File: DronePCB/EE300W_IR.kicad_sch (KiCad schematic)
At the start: 18 parts, among them Q4 AO3400A, Q5 AO3400A, U8 TSOP45xx

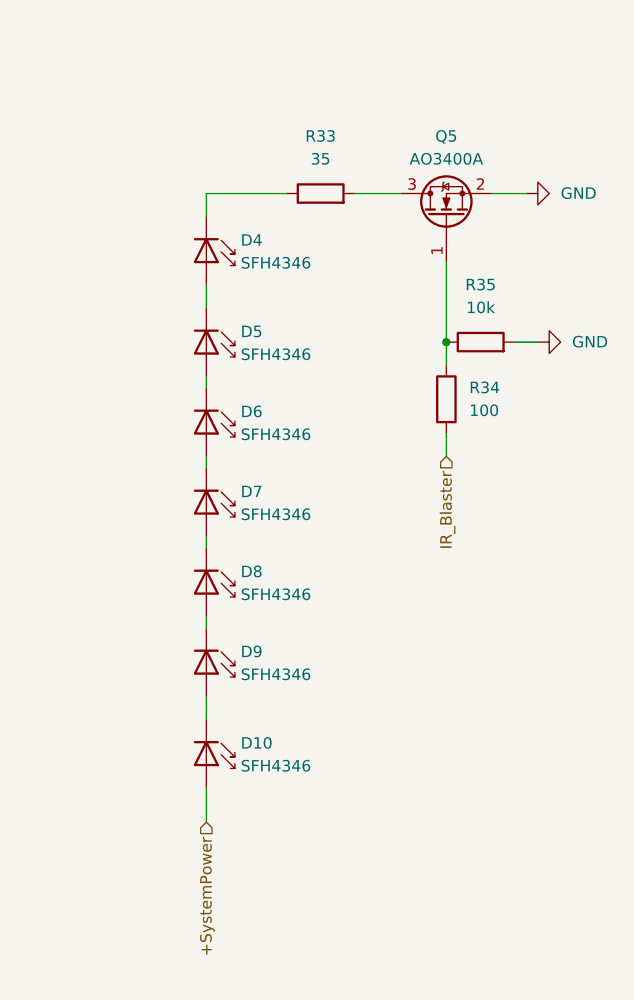
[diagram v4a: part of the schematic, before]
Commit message: Changed Resistor on IR Blaster | Finished Running DRC on PCB
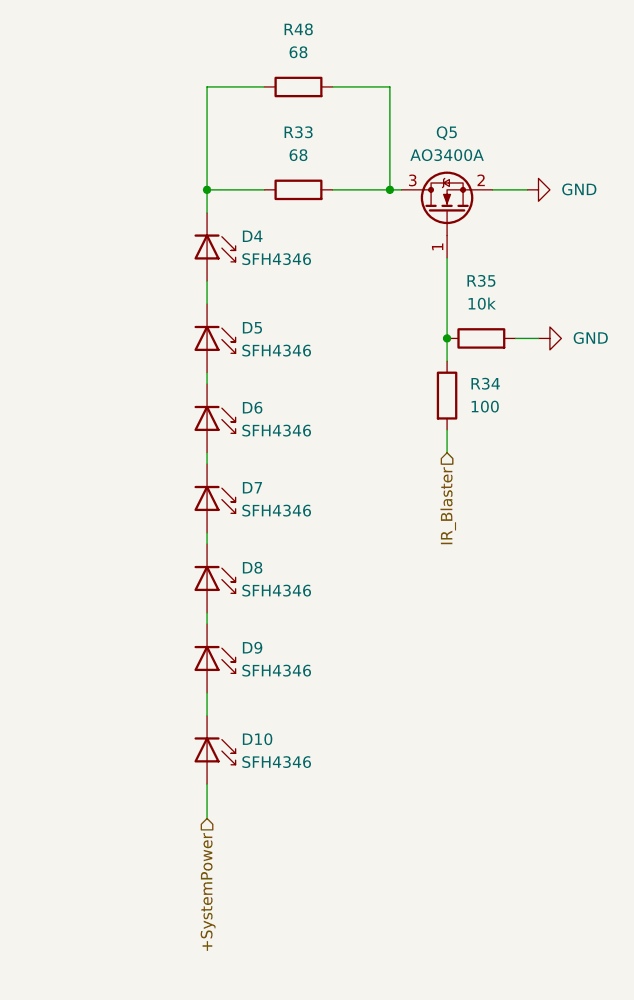
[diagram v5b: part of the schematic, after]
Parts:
- added R48: 68, Resistor_SMD:R_1206_3216Metric, symbol Device:R
- R33: value 35 -> 68; footprint Resistor_SMD:R_0603_1608Metric -> Resistor_SMD:R_1206_3216Metric
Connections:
- net at Q5.3 (D), R33.2: now also R48.2
- net at D4.1 (K), R33.1: now also R48.1
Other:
- moved on the sheet: R33
